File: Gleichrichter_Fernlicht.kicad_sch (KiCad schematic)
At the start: 16 parts, among them Q1 Q_NMOS_GDS, Q2 Q_PMOS_GDS, Q3 Q_PMOS_GDS, Q4 Q_NMOS_GDS

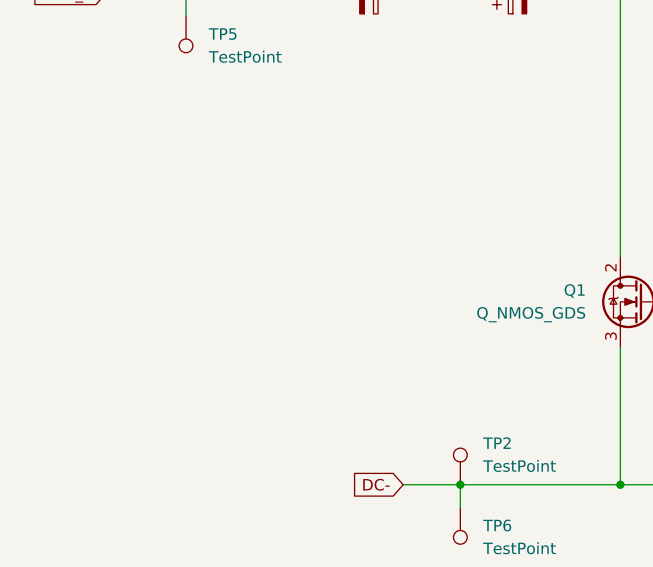
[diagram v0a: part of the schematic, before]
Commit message: Kontur von Jan importiert und gelayoutet. Evtl. noch Kupferflaechen machen?
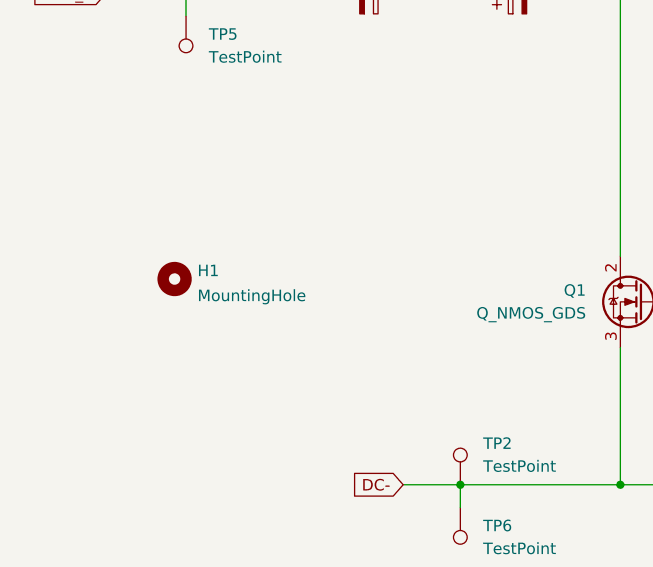
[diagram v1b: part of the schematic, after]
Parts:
- added H1: MountingHole, MountingHole:MountingHole_5mm, symbol Mechanical:MountingHole
- TP1, TP2, TP3, TP4, TP5, TP6, TP7, TP8: footprint TestPoint:TestPoint_Pad_1.5x1.5mm -> TestPoint:TestPoint_Pad_2.5x2.5mm
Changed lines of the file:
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@@
       (effects (font (size 1.27 1.27)) (justify left))
     )
-    (property "Footprint" "TestPoint:TestPoint_Pad_1.5x1.5mm" (id 2) (at 210.82 123.19 0)
+    (property "Footprint" "TestPoint:TestPoint_Pad_2.5x2.5mm" (id 2) (at 210.82 123.19 0)
       (effects (font (size 1.27 1.27)) hide)
     )
@@
       (effects (font (size 1.27 1.27)) (justify right))
     )
-    (property "Footprint" "TestPoint:TestPoint_Pad_1.5x1.5mm" (id 2) (at 92.71 121.92 0)
+    (property "Footprint" "TestPoint:TestPoint_Pad_2.5x2.5mm" (id 2) (at 92.71 121.92 0)
       (effects (font (size 1.27 1.27)) hide)
     )
@@
       (effects (font (size 1.27 1.27)) (justify left))
     )
-    (property "Footprint" "TestPoint:TestPoint_Pad_1.5x1.5mm" (id 2) (at 102.87 119.38 0)
+    (property "Footprint" "TestPoint:TestPoint_Pad_2.5x2.5mm" (id 2) (at 102.87 119.38 0)
       (effects (font (size 1.27 1.27)) hide)
     )
@@
       (effects (font (size 1.27 1.27)) (justify left))
     )
-    (property "Footprint" "TestPoint:TestPoint_Pad_1.5x1.5mm" (id 2) (at 72.39 63.5 0)
+    (property "Footprint" "TestPoint:TestPoint_Pad_2.5x2.5mm" (id 2) (at 72.39 63.5 0)
       (effects (font (size 1.27 1.27)) hide)
     )
@@
       (effects (font (size 1.27 1.27)) (justify right))
     )
-    (property "Footprint" "TestPoint:TestPoint_Pad_1.5x1.5mm" (id 2) (at 62.23 67.31 0)
+    (property "Footprint" "TestPoint:TestPoint_Pad_2.5x2.5mm" (id 2) (at 62.23 67.31 0)
       (effects (font (size 1.27 1.27)) hide)
     )
@@
     (pin "1")
   )
+  (symbol (lib_id "Mechanical:MountingHole") (at 66.04 96.52 0) (unit 1)
+    (in_bom yes) (on_board yes) (fields_autoplaced)
+    (property "Reference" "H1" (id 0) (at 68.58 95.6115 0)
+      (effects (font (size 1.27 1.27)) (justify left))
+    )
+    (property "Value" "MountingHole" (id 1) (at 68.58 98.3866 0)
+      (effects (font (size 1.27 1.27)) (justify left))
+    )
+    (property "Footprint" "MountingHole:MountingHole_5mm" (id 2) (at 66.04 96.52 0)
+      (effects (font (size 1.27 1.27)) hide)
+    )
+    (property "Datasheet" "~" (id 3) (at 66.04 96.52 0)
+      (effects (font (size 1.27 1.27)) hide)
+    )
+  )
   (symbol (lib_id "Device:Q_PMOS_GDS") (at 187.96 100.33 0) (unit 1)
     (in_bom yes) (on_board yes) (fields_autoplaced)
@@
       (effects (font (size 1.27 1.27)) (justify left))
     )
-    (property "Footprint" "TestPoint:TestPoint_Pad_1.5x1.5mm" (id 2) (at 222.25 64.77 0)
+    (property "Footprint" "TestPoint:TestPoint_Pad_2.5x2.5mm" (id 2) (at 222.25 64.77 0)
       (effects (font (size 1.27 1.27)) hide)
     )
@@
       (effects (font (size 1.27 1.27)) (justify right))
     )
-    (property "Footprint" "TestPoint:TestPoint_Pad_1.5x1.5mm" (id 2) (at 215.9 68.58 0)
+    (property "Footprint" "TestPoint:TestPoint_Pad_2.5x2.5mm" (id 2) (at 215.9 68.58 0)
       (effects (font (size 1.27 1.27)) hide)
     )
@@
       (effects (font (size 1.27 1.27)) (justify right))
     )
-    (property "Footprint" "TestPoint:TestPoint_Pad_1.5x1.5mm" (id 2) (at 200.66 125.73 0)
+    (property "Footprint" "TestPoint:TestPoint_Pad_2.5x2.5mm" (id 2) (at 200.66 125.73 0)
       (effects (font (size 1.27 1.27)) hide)
     )
@@
       (reference "D2") (unit 1) (value "ZD_16") (footprint "Diode_SMD:D_MiniMELF_Handsoldering")
     )
+    (path "/bd8b013d-e476-453b-8b6c-2aa06859db7f"
+      (reference "H1") (unit 1) (value "MountingHole") (footprint "MountingHole:MountingHole_5mm")
+    )
     (path "/34d03349-6d78-4165-a683-2d8b76f2bae8"
       (reference "Q1") (unit 1) (value "Q_NMOS_GDS") (footprint "Package_TO_SOT_SMD:SOT-23_Handsoldering")
@@
     )
     (path "/a37ca12b-5233-43ad-bbc5-eb0f992f7532"
-      (reference "TP1") (unit 1) (value "TestPoint") (footprint "TestPoint:TestPoint_Pad_1.5x1.5mm")
+      (reference "TP1") (unit 1) (value "TestPoint") (footprint "TestPoint:TestPoint_Pad_2.5x2.5mm")
     )
     (path "/71ac0761-e35f-4982-a617-c67ffde7418c"
-      (reference "TP2") (unit 1) (value "TestPoint") (footprint "TestPoint:TestPoint_Pad_1.5x1.5mm")
+      (reference "TP2") (unit 1) (value "TestPoint") (footprint "TestPoint:TestPoint_Pad_2.5x2.5mm")
     )
     (path "/1e1eade0-f92d-46a6-862d-b19804098158"
-      (reference "TP3") (unit 1) (value "TestPoint") (footprint "TestPoint:TestPoint_Pad_1.5x1.5mm")
+      (reference "TP3") (unit 1) (value "TestPoint") (footprint "TestPoint:TestPoint_Pad_2.5x2.5mm")
     )
     (path "/e044880f-603a-44a0-adba-8e2adeb203c2"
-      (reference "TP4") (unit 1) (value "TestPoint") (footprint "TestPoint:TestPoint_Pad_1.5x1.5mm")
+      (reference "TP4") (unit 1) (value "TestPoint") (footprint "TestPoint:TestPoint_Pad_2.5x2.5mm")
     )
     (path "/aca13832-4a1f-4af0-adcd-2bda79e97c00"
-      (reference "TP5") (unit 1) (value "TestPoint") (footprint "TestPoint:TestPoint_Pad_1.5x1.5mm")
+      (reference "TP5") (unit 1) (value "TestPoint") (footprint "TestPoint:TestPoint_Pad_2.5x2.5mm")
     )
     (path "/614d1fc7-a51b-45d2-89d5-4d0c0505dcde"
-      (reference "TP6") (unit 1) (value "TestPoint") (footprint "TestPoint:TestPoint_Pad_1.5x1.5mm")
+      (reference "TP6") (unit 1) (value "TestPoint") (footprint "TestPoint:TestPoint_Pad_2.5x2.5mm")
     )
     (path "/f564e0c5-8187-4a95-84fe-12a6761816e9"
-      (reference "TP7") (unit 1) (value "TestPoint") (footprint "TestPoint:TestPoint_Pad_1.5x1.5mm")
+      (reference "TP7") (unit 1) (value "TestPoint") (footprint "TestPoint:TestPoint_Pad_2.5x2.5mm")
     )
     (path "/e8795dfb-7cc2-4438-a3db-8ee41718606c"
-      (reference "TP8") (unit 1) (value "TestPoint") (footprint "TestPoint:TestPoint_Pad_1.5x1.5mm")
-    )
-  )
+      (reference "TP8") (unit 1) (value "TestPoint") (footprint "TestPoint:TestPoint_Pad_2.5x2.5mm")
+    )
+  )

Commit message: Standard Mosfet-Symbol hat nicht zu SOT-23 Footprint gepasst. (Drain und Source vertauscht). Jetzt korrigiert. Layout noch nicht fertig. Hotfix: Transistoren auf erster Platine verkehrt herum drauflöten
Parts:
- removed Q1, Q4: Q_NMOS_GDS, Package_TO_SOT_SMD:SOT-23_Handsoldering, symbol Device:Q_NMOS_GDS
- removed Q2, Q3: Q_PMOS_GDS, Package_TO_SOT_SMD:SOT-23_Handsoldering, symbol Device:Q_PMOS_GDS
- added Q1, Q3: 2N7002, Package_TO_SOT_SMD:SOT-23, symbol Transistor_FET:2N7002
- added Q2, Q4: AO3401A, Package_TO_SOT_SMD:SOT-23, symbol Transistor_FET:AO3401A
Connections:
- net DC+: now also Q2.2 (S), Q4.2 (S)
- net DC-: now also Q1.2 (S), Q3.2 (S)
- net DYN_2: now also Q1.1 (G), Q2.1 (G), Q3.3 (D), Q4.3 (D)
- net at C2.2, D1.1 (K): now also Q1.3 (D), Q2.3 (D), Q3.1 (G), Q4.1 (G)

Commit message: update: Layout korrigiert und an jlc geschickt
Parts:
- added D3, D4: ZD_16, Diode_SMD:D_MiniMELF_Handsoldering, symbol Device:D_Zener
- D1, D2: footprint Diode_SMD:D_MiniMELF_Handsoldering -> Diode_SMD:D_SOD-123
- Q1, Q2, Q3, Q4: footprint Package_TO_SOT_SMD:SOT-23 -> Package_TO_SOT_SMD:SOT-23_Handsoldering
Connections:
- net DYN_2: now also D4.1 (K)
- net at C2.2, D1.1 (K), Q1.3 (D)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: now also D3.1 (K)
- net at D1.2 (A), D2.2 (A): now also D3.2 (A), D4.2 (A)
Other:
- moved on the sheet: D2
